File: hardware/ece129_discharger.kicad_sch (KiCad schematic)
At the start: 29 parts, among them J1 Conn_01x03, J10 Conn_01x02, J11 Conn_02x05_Top_Bottom, J12 Conn_01x08, J13 Conn_02x05_Top_Bottom, J14 Conn_01x02, J15 Conn_01x02, J16 Conn_01x08, J17 Conn_01x02, J18 Conn_01x02, J2 Conn_01x02, J3 Conn_01x02, J4 Conn_01x02, J5 Conn_01x02, J6 Conn_01x02, J7 Conn_01x02, J8 Conn_01x02, J9 Conn_01x02, Q2 AO3400A, SW1 SW_Push, U6 VX7805-500, U7 ISO1050DUB

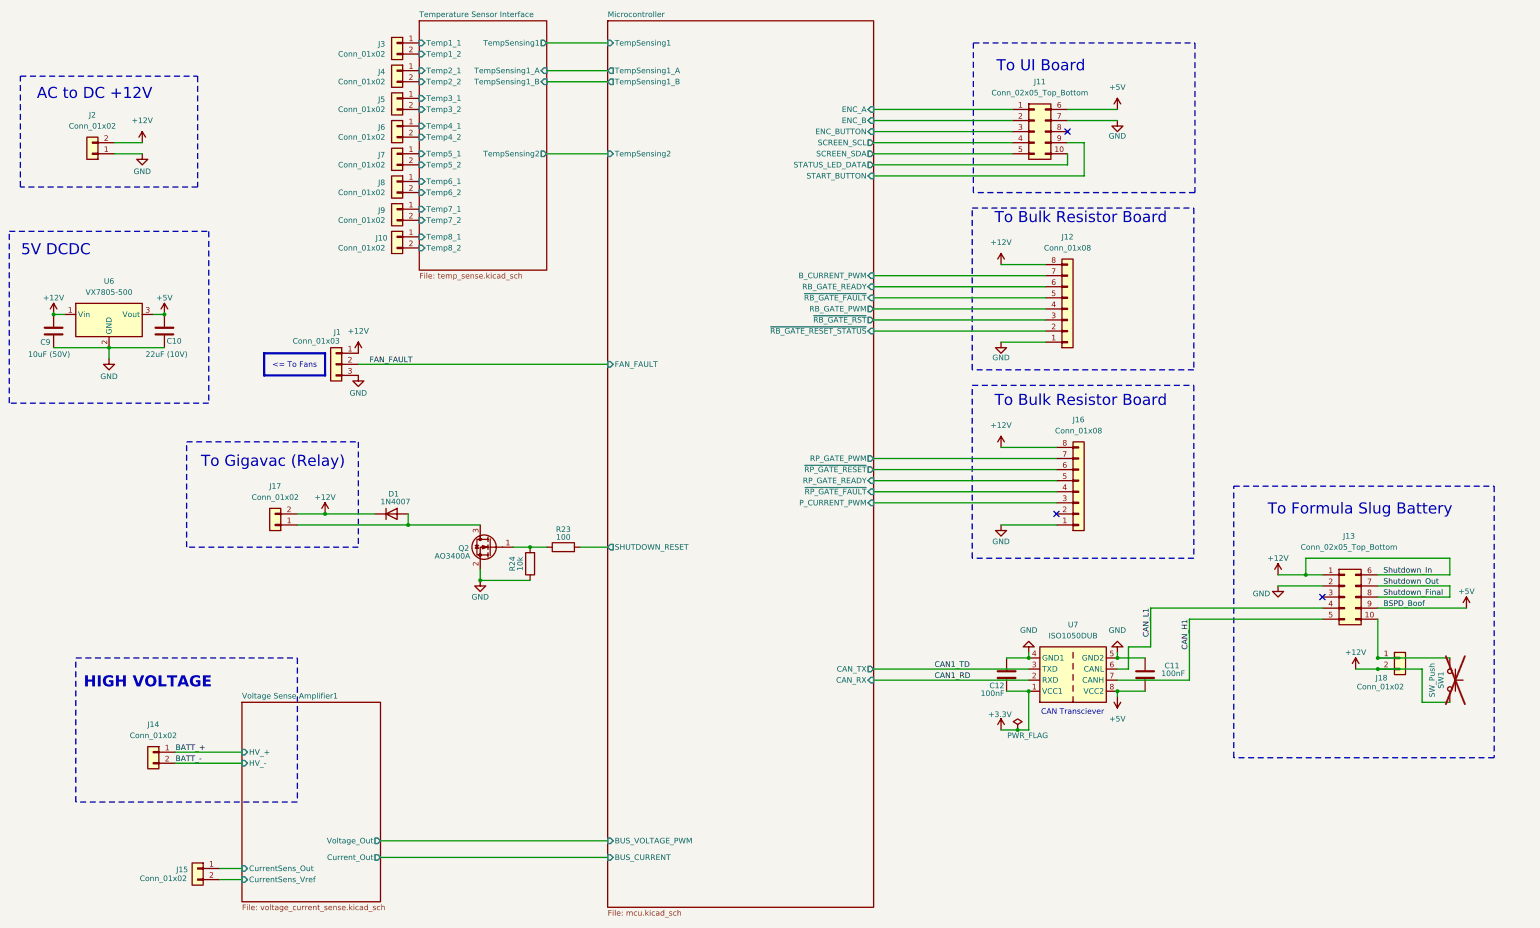
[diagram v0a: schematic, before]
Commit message: initial layout, power traces remain
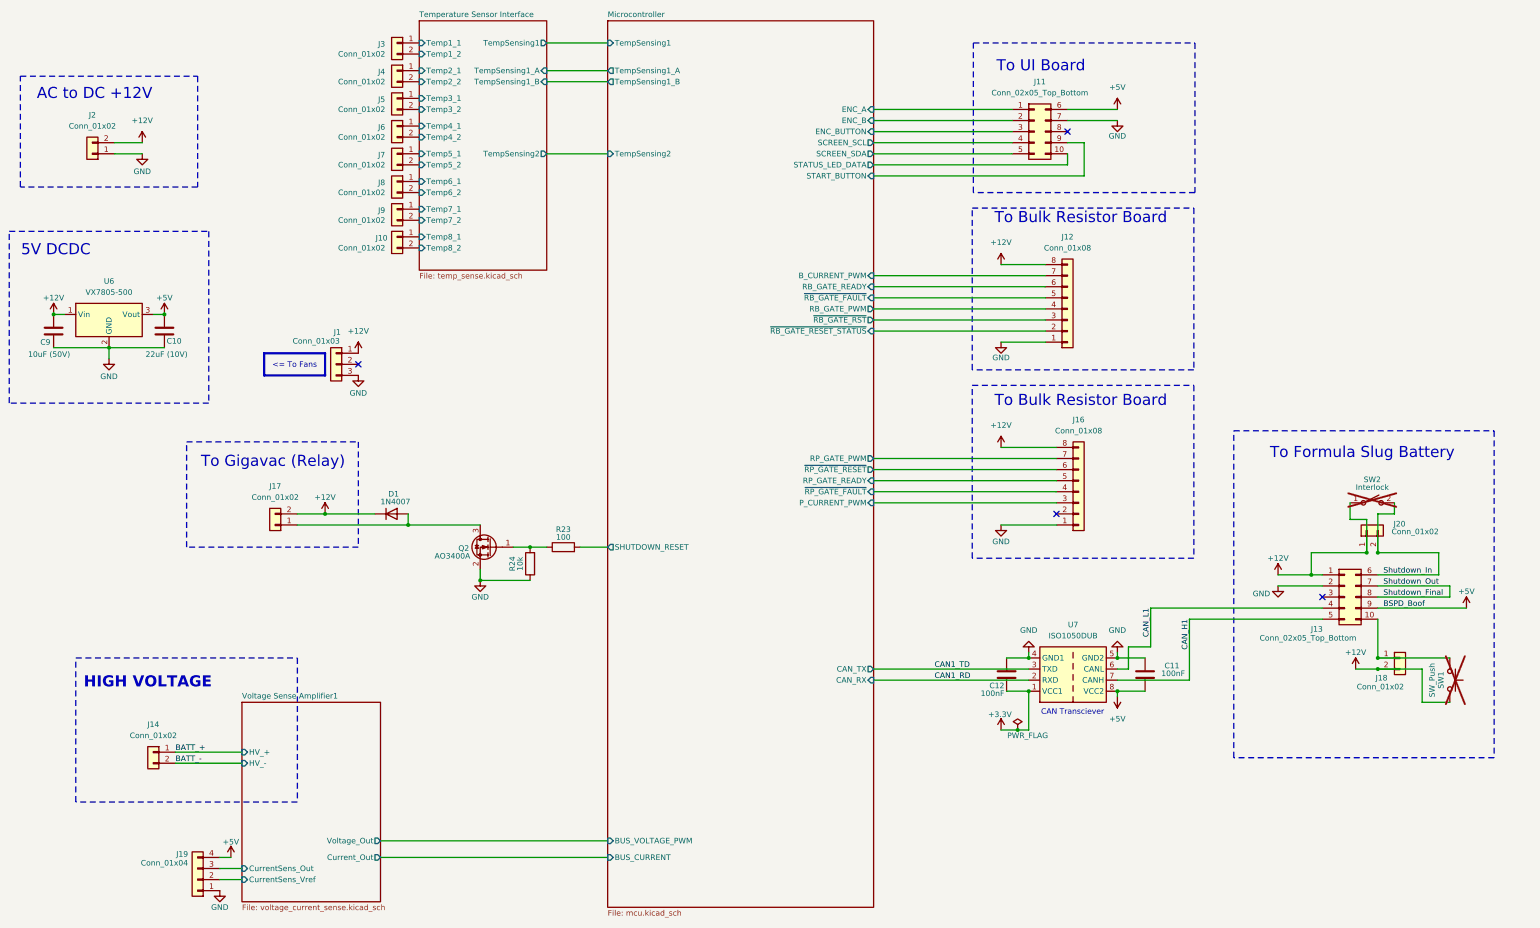
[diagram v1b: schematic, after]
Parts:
- removed J15: Conn_01x02, symbol Connector_Generic:Conn_01x02
- added J19: Conn_01x04, Connector_Molex:Molex_Nano-Fit_105309-xx04_1x04_P2.50mm_Vertical, symbol Connector_Generic:Conn_01x04
- added J20: Conn_01x02, Connector_Molex:Molex_Nano-Fit_105309-xx02_1x02_P2.50mm_Vertical, symbol Connector_Generic:Conn_01x02
- added SW2: Interlock, symbol Switch:SW_SPST
- C10, C9: footprint (none) -> Capacitor_SMD:C_0805_2012Metric_Pad1.18x1.45mm_HandSolder
- J1: footprint (none) -> Connector_Molex:Molex_Nano-Fit_105309-xx03_1x03_P2.50mm_Vertical
- J10, J14, J17, J18, J2, J3, J4, J5, J6, J7, J8, J9: footprint (none) -> Connector_Molex:Molex_Nano-Fit_105309-xx02_1x02_P2.50mm_Vertical
- J11, J13: footprint (none) -> Connector_Molex:Molex_Nano-Fit_105310-xx10_2x05_P2.50mm_Vertical
- J12, J16: footprint (none) -> Connector_Molex:Molex_Nano-Fit_105309-xx08_1x08_P2.50mm_Vertical
- R23, R24: footprint (none) -> Resistor_SMD:R_0805_2012Metric_Pad1.20x1.40mm_HandSolder
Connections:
- net +12V: now also J20.1 (Pin_1), SW2.1 (A); no longer J13.6 (Pin_6)
- net +5V: now also J19.4 (Pin_4)
- net GND: now also J19.1 (Pin_1)
- net Voltage Sense Amplifier1/CurrentSens_Out: now also J19.3 (Pin_3)
- net Voltage Sense Amplifier1/CurrentSens_Vref: now also J19.2 (Pin_2)
- net FAN_FAULT: no longer names the net of J1.2 (Pin_2)
- new net Shutdown_In: J13.6 (Pin_6), J20.2 (Pin_2), SW2.2 (B)
- no-connect marks 3 -> 4
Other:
- sheet Microcontroller ports: added none; removed FAN_FAULT

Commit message: Finished Layout and routing
* Flipped CAN transceiver upside down on schematic
* Moved CAN transceiver nearer to J13 and MCU CAN pins
* Moved 5V DCDC caps nearer to 5V DCDC
* Moved Silkscreen out from under U9
* Moved J2 and J1 to prevent plugging 12V into a temp sensor connector
* Change +3.3V to +3V3 to match MCU page
* Changed Current Sense circuit to use U4D, sharing with Temp Sense (for easier assembly)
* Placed Unused MCP6004s on schematic and connected them per datasheet fig 4-5
* Remove connections to HV- in Current Sensing (Replaced with GND)
* Tightened up Temp and Current Sense amplifier layouts
* Swap U15A with U15D for easier routing
* Added buffer to voltage sense circuit because filter stage could significantly load the voltage divider
* Added a smattering of decoupling caps
* Finished Layout and routing
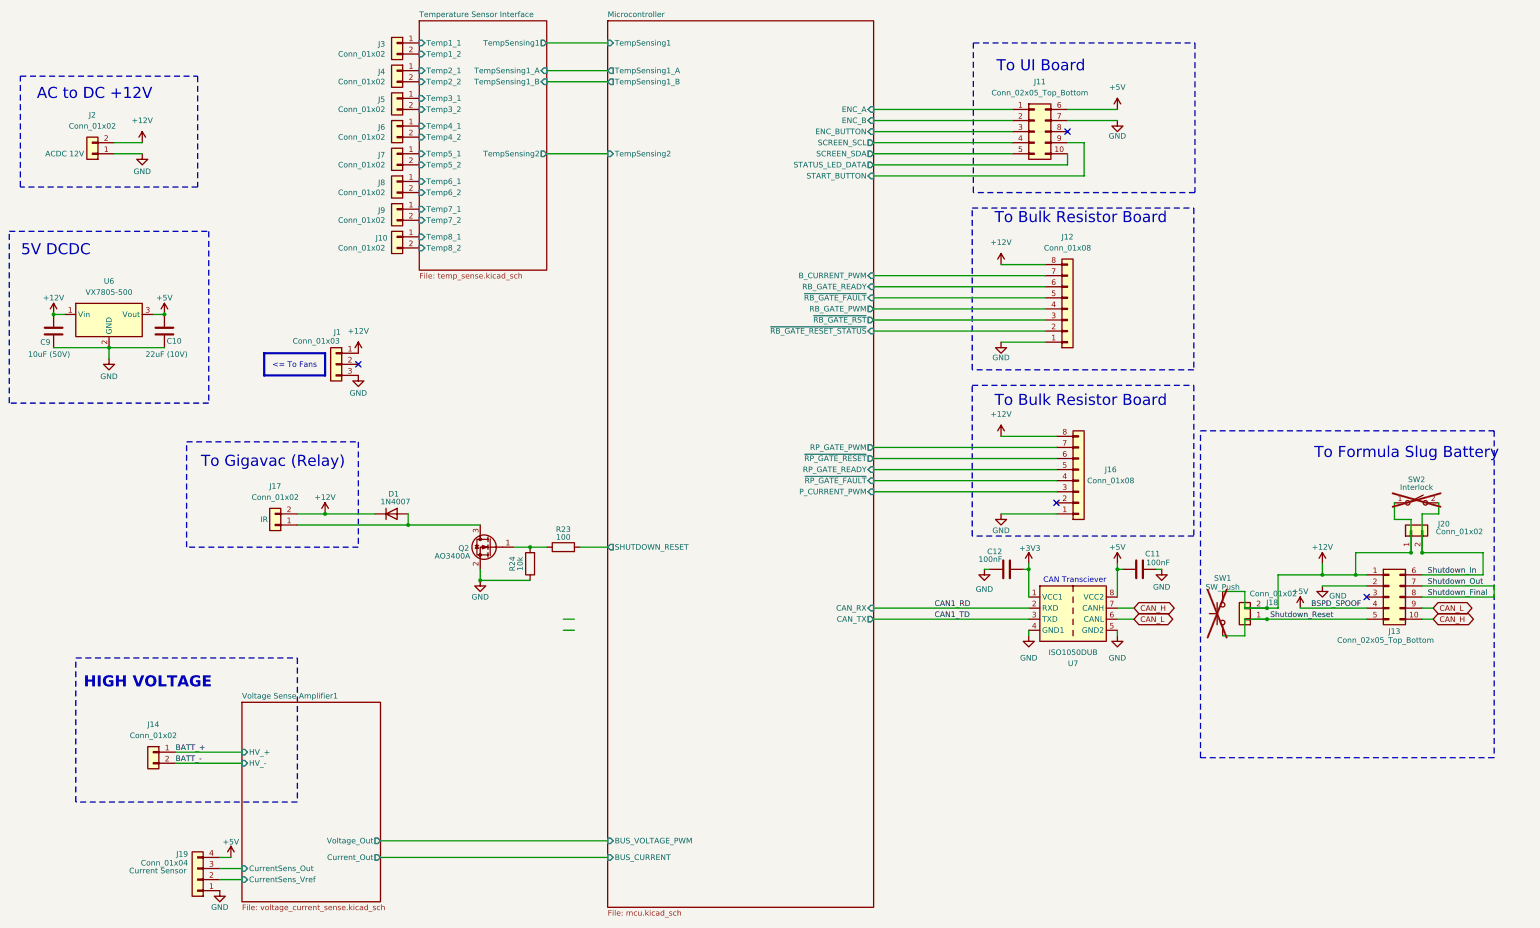
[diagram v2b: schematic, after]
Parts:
- C10, C11, C12, C9, R23, R24: KiLib_Generator (none) -> SMD_2terminal_chip_molded
- D1: KiLib_Generator (none) -> diode/THT
- J1, J10, J11, J12, J14, J16, J3, J4, J5, J6, J7, J8, J9: KiLib_Generator (none) -> connector/Molex
- J13: KiLib_Generator (none) -> connector/Molex; Name (none) -> Accumulator SFC
- J17: KiLib_Generator (none) -> connector/Molex; Name (none) -> IR
- J18: KiLib_Generator (none) -> connector/Molex; Name (none) -> Shutdown Reset
- J19: KiLib_Generator (none) -> connector/Molex; Name (none) -> Current Sensor
- J2: KiLib_Generator (none) -> connector/Molex; Name (none) -> ACDC 12V
- J20: KiLib_Generator (none) -> connector/Molex; Name (none) -> Shutdown Interlock
- Q2, U7: KiLib_Generator (none) -> package/gullwing
- U6: KiLib_Generator (none) -> converter_ACDC_DCDC
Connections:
- net +12V: now also SW1.1; no longer SW1.2
- net +5V: now also J13.4 (Pin_4); no longer J13.9 (Pin_9)
- net +3.3V renamed +3V3
- net CAN_H1 renamed CAN_H
- net CAN_H: now also J13.10 (Pin_10); no longer J13.5 (Pin_5)
- net CAN_L1 renamed CAN_L
- net CAN_L: now also J13.9 (Pin_9); no longer J13.4 (Pin_4)
- new net Shutdown_Reset: J13.5 (Pin_5), J18.1 (Pin_1), SW1.2
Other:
- moved on the sheet: C11, C12, J13, J16, J20, SW2, U7
